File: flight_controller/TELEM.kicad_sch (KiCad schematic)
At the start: 28 parts, among them J11 A1257WV-S-6P-LCP, J5 A1257WV-S-6P-LCP, J6 A1257WV-S-6P-LCP, J7 A1257WV-S-6P-LCP, J8 SM04B-SRSS-TB(LF)(SN)

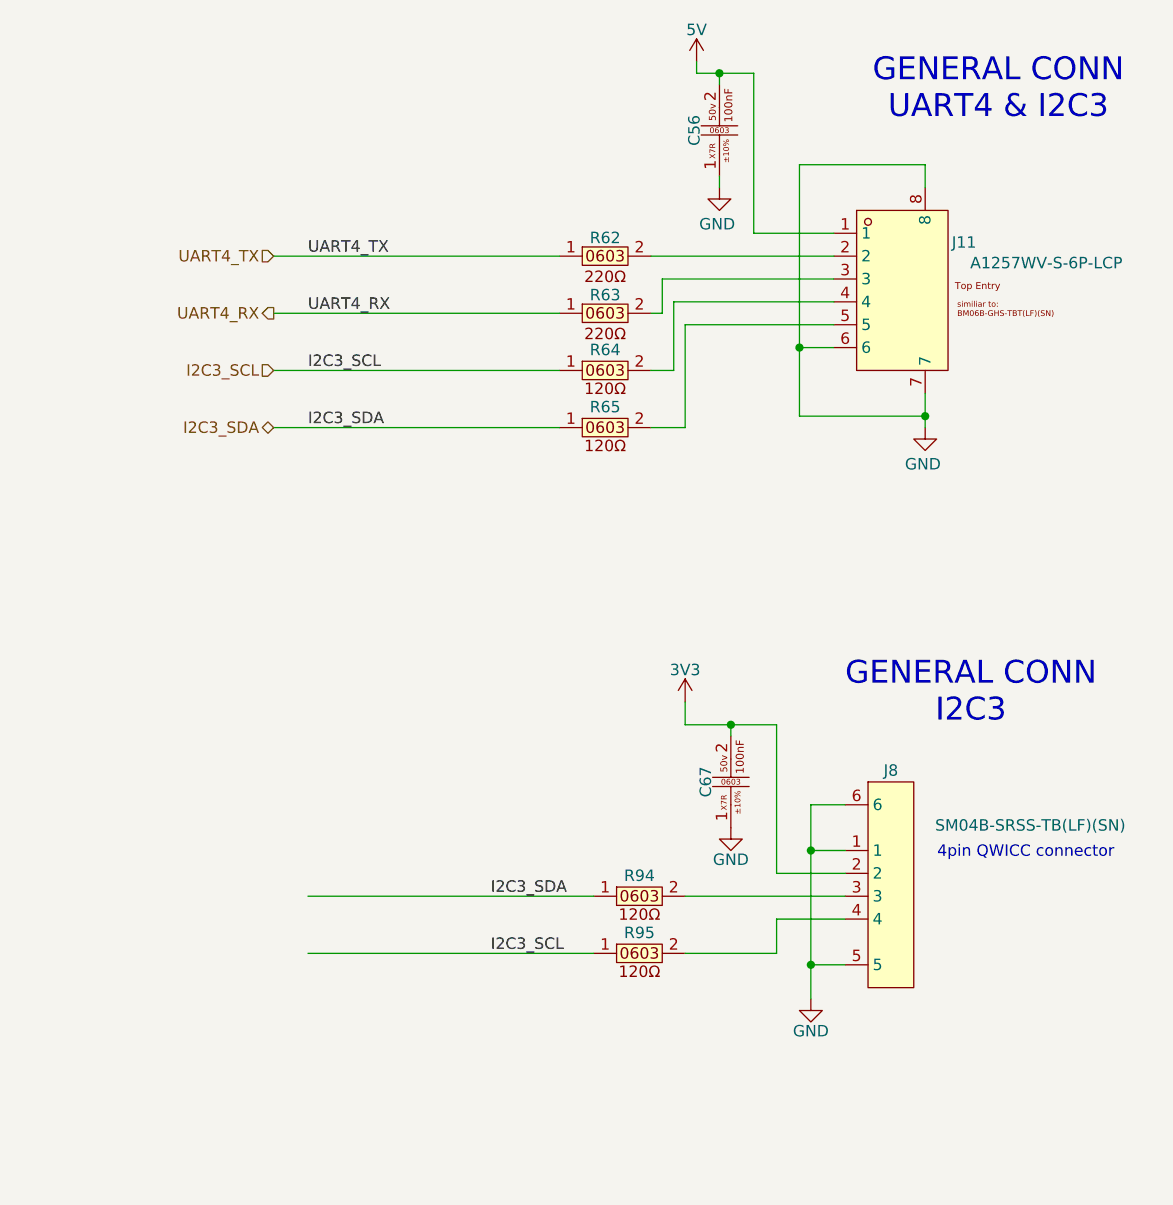
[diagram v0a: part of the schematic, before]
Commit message: Schematic complete, ready for layout. Added USB, TPs, power conn, updated clocks, ran Rules Checker and general review
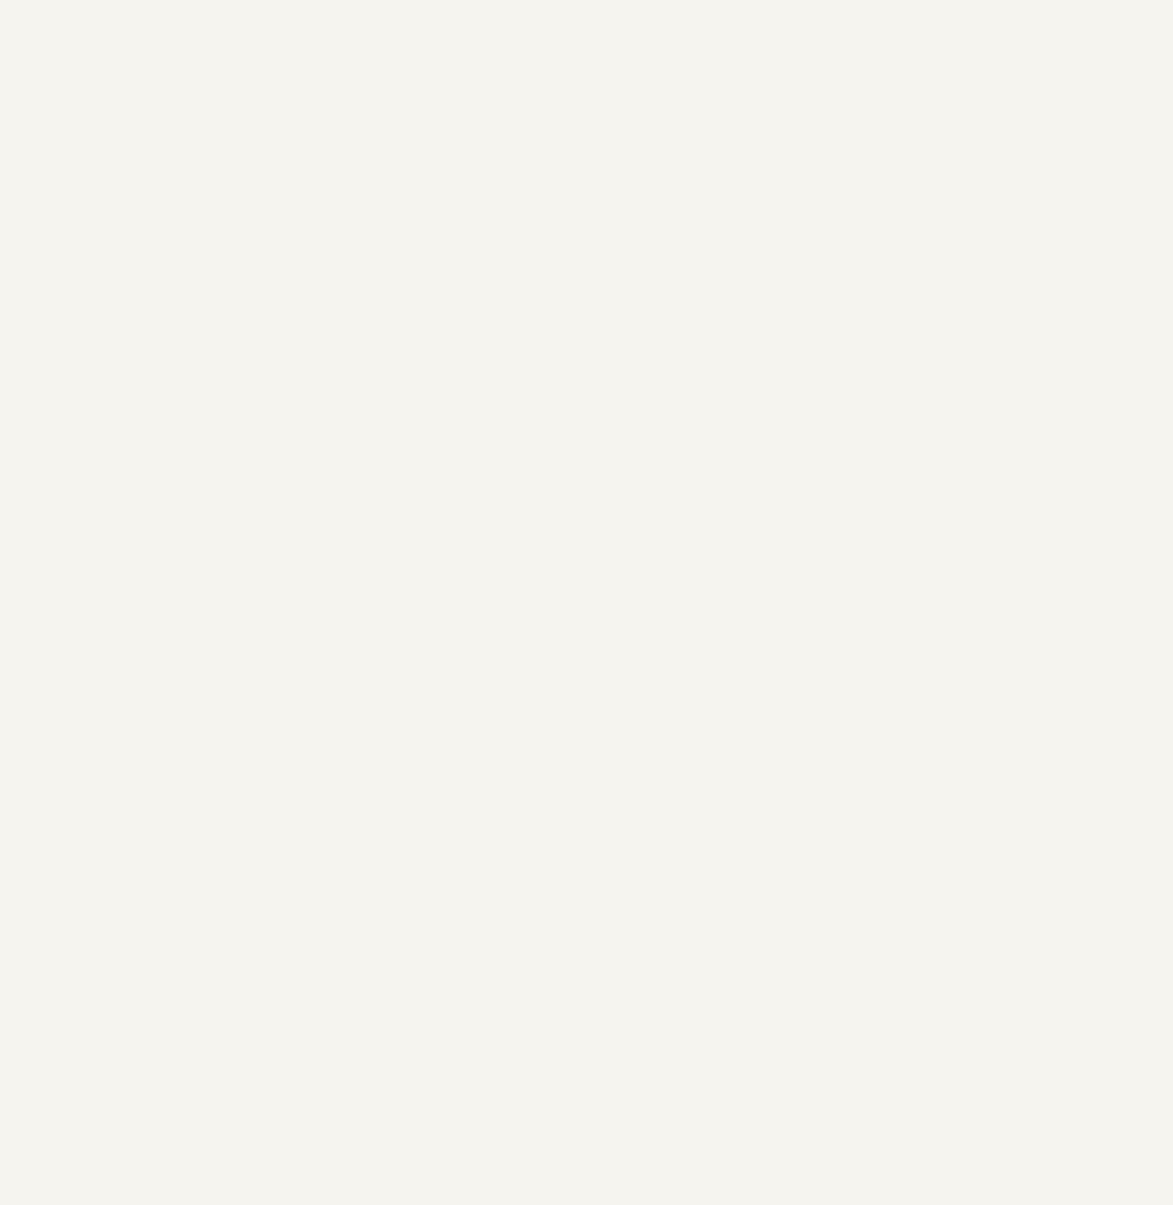
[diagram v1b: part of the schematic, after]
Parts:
- removed C56, C67: CC0603KRX7R9BB104 (100nf , 0603 ,50v ,X7R), easyeda2kicad:C0603, symbol lampelKicadLIB:CC0603KRX7R9BB104 (100nf , 0603 ,50v ,X7R)
- removed J11: A1257WV-S-6P-LCP, easyeda2kicad:CONN-SMD_A1257WV-S-6P, symbol lampelKicadLIB:A1257WV-S-6P-LCP
- removed J8: SM04B-SRSS-TB(LF)(SN), easyeda2kicad:CONN-SMD_4P-P1.00_SM04B-SRSS-TB-LF-SN, symbol lampelKicadLIB:SM04B-SRSS-TB(LF)(SN) (4pin QWICC connector USE THIS )
- removed R62, R63: 0603WAF2200T5E (220ohm , 0603), easyeda2kicad:R0603, symbol lampelKicadLIB:0603WAF2200T5E (220ohm , 0603)
- removed R64, R65, R94, R95: 603WAF1200T5E, easyeda2kicad:R0603, symbol lampelKicadLIB:0603WAF1200T5E (120ohm,0603)
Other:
- note removed: "4pin QWICC connector"
- note removed: "GENERAL CONN I2C3"
- note removed: "GENERAL CONN UART4 & I2C3"

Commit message: Started the placement process
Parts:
- renumbered C44 to C60, C48 to C61, C43 to C62, J6 to J11, J7 to J12, J5 to J13, R34 to R59, R35 to R60, R38 to R61, R39 to R62, R40 to R63, R41 to R64, R42 to R65, R43 to R66, R9 to R67, R10 to R68, R11 to R69, R12 to R70

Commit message: Updated power and usb connectors, annotations and netlist check
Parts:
- renumbered J11 to J13, J12 to J14, J13 to J15, R59 to R58, R60 to R59, R61 to R60, R62 to R61, R63 to R62, R64 to R63, R65 to R64, R66 to R65, R67 to R66, R68 to R67, R69 to R68, R70 to R69
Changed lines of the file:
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@@
-		(polyline
-			(pts
-				(xy 68.58 129.54) (xy 68.58 181.61) (xy 148.59 181.61) (xy 148.59 129.54)
-			)
-			(stroke
-				(width 0)
-				(type dash)
-			)
-			(fill
-				(type none)
-			)
-		)
-	)
-	(rule_area
 		(polyline
 			(pts
@@
 			(pts
 				(xy 79.375 74.93) (xy 79.375 127) (xy 173.99 127.635) (xy 173.99 74.93)
+			)
+			(stroke
+				(width 0)
+				(type dash)
+			)
+			(fill
+				(type none)
+			)
+		)
+	)
+	(rule_area
+		(polyline
+			(pts
+				(xy 68.58 129.54) (xy 68.58 181.61) (xy 148.59 181.61) (xy 148.59 129.54)
 			)
 			(stroke
@@
 		(dnp no)
 		(fields_autoplaced yes)
-		(property "Reference" "R65"
+		(property "Reference" "R64"
 			(at 85.09 166.878 0)
 			(do_not_autoplace yes)
@@
 			(project "FP_BOARD"
 				(path "/17737359-1a8e-4237-8899-d9604030bc1d/ee742a7d-8184-434b-840f-4020f45cd711"
-					(reference "R65")
+					(reference "R64")
 					(unit 1)
 				)
@@
 		(on_board yes)
 		(dnp no)
-		(property "Reference" "#PWR0160"
+		(property "Reference" "#PWR0158"
 			(at 95.25 138.43 0)
 			(effects
@@
 			(project "FP_BOARD"
 				(path "/17737359-1a8e-4237-8899-d9604030bc1d/ee742a7d-8184-434b-840f-4020f45cd711"
-					(reference "#PWR0160")
+					(reference "#PWR0158")
 					(unit 1)
 				)
@@
 		(dnp no)
 		(fields_autoplaced yes)
-		(property "Reference" "R66"
+		(property "Reference" "R65"
 			(at 85.09 173.228 0)
 			(do_not_autoplace yes)
@@
 			(project "FP_BOARD"
 				(path "/17737359-1a8e-4237-8899-d9604030bc1d/ee742a7d-8184-434b-840f-4020f45cd711"
-					(reference "R66")
+					(reference "R65")
 					(unit 1)
 				)
@@
 		(dnp no)
 		(fields_autoplaced yes)
-		(property "Reference" "R61"
+		(property "Reference" "R60"
 			(at 85.09 112.268 0)
 			(do_not_autoplace yes)
@@
 			(project "FP_BOARD"
 				(path "/17737359-1a8e-4237-8899-d9604030bc1d/ee742a7d-8184-434b-840f-4020f45cd711"
-					(reference "R61")
+					(reference "R60")
 					(unit 1)
 				)
@@
 		(dnp no)
 		(fields_autoplaced yes)
-		(property "Reference" "R63"
+		(property "Reference" "R62"
 			(at 85.09 154.178 0)
 			(do_not_autoplace yes)
@@
 			(project "FP_BOARD"
 				(path "/17737359-1a8e-4237-8899-d9604030bc1d/ee742a7d-8184-434b-840f-4020f45cd711"
-					(reference "R63")
+					(reference "R62")
 					(unit 1)
 				)
@@
 		(dnp no)
 		(fields_autoplaced yes)
-		(property "Reference" "J11"
+		(property "Reference" "J13"
 			(at 124.968 100.076 0)
 			(do_not_autoplace yes)
@@
 			(project "FP_BOARD"
 				(path "/17737359-1a8e-4237-8899-d9604030bc1d/ee742a7d-8184-434b-840f-4020f45cd711"
-					(reference "J11")
+					(reference "J13")
 					(unit 1)
 				)
@@
 		(dnp no)
 		(fields_autoplaced yes)
-		(property "Reference" "J13"
+		(property "Reference" "J15"
 			(at 126.238 45.466 0)
 			(do_not_autoplace yes)
@@
 			(project "FP_BOARD"
 				(path "/17737359-1a8e-4237-8899-d9604030bc1d/ee742a7d-8184-434b-840f-4020f45cd711"
-					(reference "J13")
+					(reference "J15")
 					(unit 1)
 				)
@@
 		(on_board yes)
 		(dnp no)
-		(property "Reference" "#PWR0159"
+		(property "Reference" "#PWR0157"
 			(at 95.25 83.82 0)
 			(effects
@@
 			(project "FP_BOARD"
 				(path "/17737359-1a8e-4237-8899-d9604030bc1d/ee742a7d-8184-434b-840f-4020f45cd711"
-					(reference "#PWR0159")
+					(reference "#PWR0157")
 					(unit 1)
 				)
@@
 		(dnp no)
 		(fields_autoplaced yes)
-		(property "Reference" "J12"
+		(property "Reference" "J14"
 			(at 124.968 154.686 0)
 			(do_not_autoplace yes)
@@
 			(project "FP_BOARD"
 				(path "/17737359-1a8e-4237-8899-d9604030bc1d/ee742a7d-8184-434b-840f-4020f45cd711"
-					(reference "J12")
+					(reference "J14")
 					(unit 1)
 				)
@@
 		(dnp no)
 		(fields_autoplaced yes)
-		(property "Reference" "R64"
+		(property "Reference" "R63"
 			(at 85.09 160.528 0)
 			(do_not_autoplace yes)
@@
 			(project "FP_BOARD"
 				(path "/17737359-1a8e-4237-8899-d9604030bc1d/ee742a7d-8184-434b-840f-4020f45cd711"
-					(reference "R64")
+					(reference "R63")
 					(unit 1)
 				)
@@
 		(dnp no)
 		(fields_autoplaced yes)
-		(property "Reference" "R70"
+		(property "Reference" "R69"
 			(at 86.36 64.008 0)
 			(do_not_autoplace yes)
@@
 			(project "FP_BOARD"
 				(path "/17737359-1a8e-4237-8899-d9604030bc1d/ee742a7d-8184-434b-840f-4020f45cd711"
-					(reference "R70")
+					(reference "R69")
 					(unit 1)
 				)
@@
 		(on_board yes)
 		(dnp no)
-		(property "Reference" "#PWR0163"
+		(property "Reference" "#PWR0161"
 			(at 97.79 154.94 0)
 			(effects
@@
 			(project "FP_BOARD"
 				(path "/17737359-1a8e-4237-8899-d9604030bc1d/ee742a7d-8184-434b-840f-4020f45cd711"
-					(reference "#PWR0163")
+					(reference "#PWR0161")
 					(unit 1)
 				)
@@
 		(dnp no)
 		(fields_autoplaced yes)
-		(property "Reference" "R67"
+		(property "Reference" "R66"
 			(at 86.36 44.958 0)
 			(do_not_autoplace yes)
@@
 			(project "FP_BOARD"
 				(path "/17737359-1a8e-4237-8899-d9604030bc1d/ee742a7d-8184-434b-840f-4020f45cd711"
-					(reference "R67")
+					(reference "R66")
 					(unit 1)
 				)
@@
 		(dnp no)
 		(fields_autoplaced yes)
-		(property "Reference" "R62"
+		(property "Reference" "R61"
 			(at 85.09 118.618 0)
 			(do_not_autoplace yes)
@@
 			(project "FP_BOARD"
 				(path "/17737359-1a8e-4237-8899-d9604030bc1d/ee742a7d-8184-434b-840f-4020f45cd711"
-					(reference "R62")
+					(reference "R61")
 					(unit 1)
 				)
@@
 		(dnp no)
 		(fields_autoplaced yes)
-		(property "Reference" "R59"
+		(property "Reference" "R58"
 			(at 85.09 99.568 0)
 			(do_not_autoplace yes)
@@
 			(project "FP_BOARD"
 				(path "/17737359-1a8e-4237-8899-d9604030bc1d/ee742a7d-8184-434b-840f-4020f45cd711"
-					(reference "R59")
+					(reference "R58")
 					(unit 1)
 				)
@@
 		(on_board yes)
 		(dnp no)
-		(property "Reference" "#PWR0166"
+		(property "Reference" "#PWR0164"
 			(at 120.65 181.61 0)
 			(effects
@@
 			(project "FP_BOARD"
 				(path "/17737359-1a8e-4237-8899-d9604030bc1d/ee742a7d-8184-434b-840f-4020f45cd711"
-					(reference "#PWR0166")
+					(reference "#PWR0164")
 					(unit 1)
 				)
@@
 		(on_board yes)
 		(dnp no)
-		(property "Reference" "#PWR0162"
+		(property "Reference" "#PWR0160"
 			(at 97.79 100.33 0)
 			(effects
@@
 			(project "FP_BOARD"
 				(path "/17737359-1a8e-4237-8899-d9604030bc1d/ee742a7d-8184-434b-840f-4020f45cd711"
-					(reference "#PWR0162")
+					(reference "#PWR0160")
 					(unit 1)
 				)
@@
 		(dnp no)
 		(fields_autoplaced yes)
-		(property "Reference" "R68"
+		(property "Reference" "R67"
 			(at 86.36 51.308 0)
 			(do_not_autoplace yes)
@@
 			(project "FP_BOARD"
 				(path "/17737359-1a8e-4237-8899-d9604030bc1d/ee742a7d-8184-434b-840f-4020f45cd711"
-					(reference "R68")
+					(reference "R67")
 					(unit 1)
 				)
@@
 		(dnp no)
 		(fields_autoplaced yes)
-		(property "Reference" "R69"
+		(property "Reference" "R68"
 			(at 86.36 57.658 0)
 			(do_not_autoplace yes)
@@
 			(project "FP_BOARD"
 				(path "/17737359-1a8e-4237-8899-d9604030bc1d/ee742a7d-8184-434b-840f-4020f45cd711"
-					(reference "R69")
+					(reference "R68")
 					(unit 1)
 				)
@@
 		(on_board yes)
 		(dnp no)
-		(property "Reference" "#PWR0165"
+		(property "Reference" "#PWR0163"
 			(at 120.65 127 0)
 			(effects
@@
 			(project "FP_BOARD"
 				(path "/17737359-1a8e-4237-8899-d9604030bc1d/ee742a7d-8184-434b-840f-4020f45cd711"
-					(reference "#PWR0165")
+					(reference "#PWR0163")
 					(unit 1)
 				)
@@
 		(dnp no)
 		(fields_autoplaced yes)
-		(property "Reference" "R60"
+		(property "Reference" "R59"
 			(at 85.09 105.918 0)
 			(do_not_autoplace yes)
@@
 			(project "FP_BOARD"
 				(path "/17737359-1a8e-4237-8899-d9604030bc1d/ee742a7d-8184-434b-840f-4020f45cd711"
-					(reference "R60")
+					(reference "R59")
 					(unit 1)
 				)
@@
 		(on_board yes)
 		(dnp no)
-		(property "Reference" "#PWR0164"
+		(property "Reference" "#PWR0162"
 			(at 99.06 45.72 0)
 			(effects
@@
 			(project "FP_BOARD"
 				(path "/17737359-1a8e-4237-8899-d9604030bc1d/ee742a7d-8184-434b-840f-4020f45cd711"
-					(reference "#PWR0164")
+					(reference "#PWR0162")
 					(unit 1)
 				)
@@
 		(on_board yes)
 		(dnp no)
-		(property "Reference" "#PWR0161"
+		(property "Reference" "#PWR0159"
 			(at 96.52 29.21 0)
 			(effects
@@
 			(project "FP_BOARD"
 				(path "/17737359-1a8e-4237-8899-d9604030bc1d/ee742a7d-8184-434b-840f-4020f45cd711"
-					(reference "#PWR0161")
+					(reference "#PWR0159")
 					(unit 1)
 				)
@@
 		(on_board yes)
 		(dnp no)
-		(property "Reference" "#PWR0167"
+		(property "Reference" "#PWR0165"
 			(at 121.92 72.39 0)
 			(effects
@@
 			(project "FP_BOARD"
 				(path "/17737359-1a8e-4237-8899-d9604030bc1d/ee742a7d-8184-434b-840f-4020f45cd711"
-					(reference "#PWR0167")
-					(unit 1)
-				)
+					(reference "#PWR0165")
+					(unit 1)
+				)
